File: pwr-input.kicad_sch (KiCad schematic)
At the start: 14 parts, among them J5 Conn_01x02, U6 TPS259472A

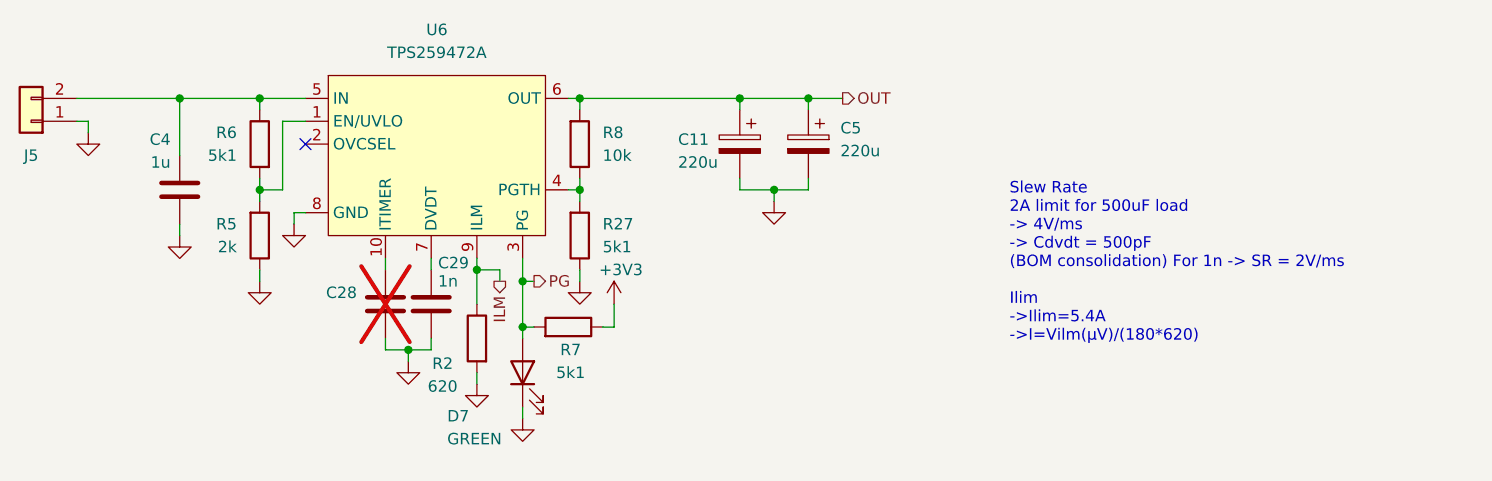
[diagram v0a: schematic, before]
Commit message: schem: add dual 5v pwr inputs
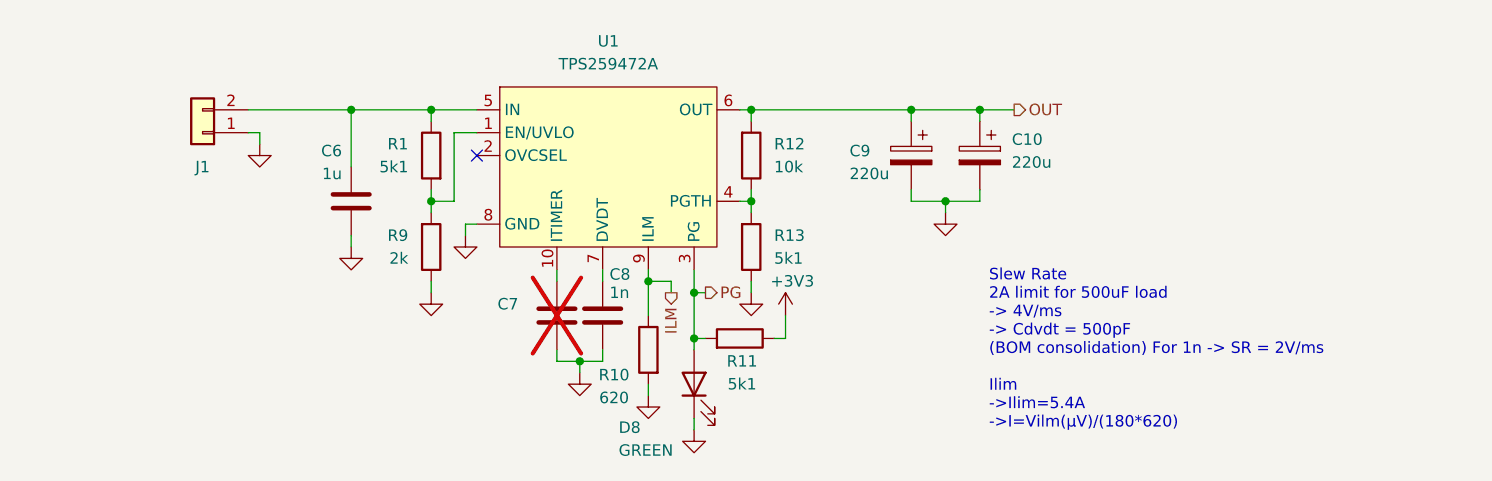
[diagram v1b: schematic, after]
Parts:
- renumbered C5 to C10, C4 to C6, C28 to C7, C29 to C8, C11 to C9, D7 to D8, J5 to J1, R6 to R1, R2 to R10, R7 to R11, R8 to R12, R27 to R13, R5 to R9, U6 to U1
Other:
- moved on the sheet: C10, C6, C7, C8, C9, D8, J1, R1, R10, R11, R12, R13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

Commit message: schem: run and fix ERC
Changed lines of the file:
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@@
+		(color 0 0 0 0)
+	)
+	(junction
+		(at 110.49 83.82)
+		(diameter 0)
 		(color 0 0 0 0)
 	)
@@
 	(wire
 		(pts
-			(xy 107.95 83.82) (xy 119.38 83.82)
+			(xy 107.95 83.82) (xy 110.49 83.82)
 		)
 		(stroke
@@
 		(pts
 			(xy 147.32 101.6) (xy 147.32 102.87)
+		)
+		(stroke
+			(width 0)
+			(type default)
+		)
+	)
+	(wire
+		(pts
+			(xy 110.49 83.82) (xy 119.38 83.82)
 		)
 		(stroke
@@
 					(unit 1)
 				)
+			)
+		)
+	)
+	(symbol
+		(lib_id "power:PWR_FLAG")
+		(at 110.49 83.82 0)
+		(unit 1)
+		(exclude_from_sim no)
+		(in_bom yes)
+		(on_board yes)
+		(dnp no)
+		(fields_autoplaced yes)
+		(property "Reference" "#FLG02"
+			(at 110.49 81.915 0)
+			(effects
+				(font
+					(size 1.27 1.27)
+				)
+				(hide yes)
+			)
+		)
+		(property "Value" "PWR_FLAG"
+			(at 110.49 78.74 0)
+			(effects
+				(font
+					(size 1.27 1.27)
+				)
+				(hide yes)
+			)
+		)
+		(property "Footprint" ""
+			(at 110.49 83.82 0)
+			(effects
+				(font
+					(size 1.27 1.27)
+				)
+				(hide yes)
+			)
+		)
+		(property "Datasheet" "~"
+			(at 110.49 83.82 0)
+			(effects
+				(font
+					(size 1.27 1.27)
+				)
+				(hide yes)
+			)
+		)
+		(property "Description" "Special symbol for telling ERC where power comes from"
+			(at 110.49 83.82 0)
+			(effects
+				(font
+					(size 1.27 1.27)
+				)
+				(hide yes)
+			)
+		)
+		(pin "1"
+		)
+		(instances
+			(project "valrob-carte-actionneurs-cdf-1"
+				(path "/6d04427e-e45e-4b7f-8323-501f87acc543/893ee43e-1e1d-4b28-9f3e-05e35ba62aed"
+					(reference "#FLG03")
+					(unit 1)
+				)
+				(path "/6d04427e-e45e-4b7f-8323-501f87acc543/fbcc9a91-3664-4a13-b680-428e68f2e4f4"
+					(reference "#FLG02")
+					(unit 1)
+				)

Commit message: schem: reannotate
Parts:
- renumbered C6 to C30, C7 to C31, C8 to C32, C9 to C33, C10 to C34, D8 to D26, J1 to J5, R1 to R13, R9 to R14, R10 to R15, R11 to R16, R12 to R17, R13 to R18, U1 to U4

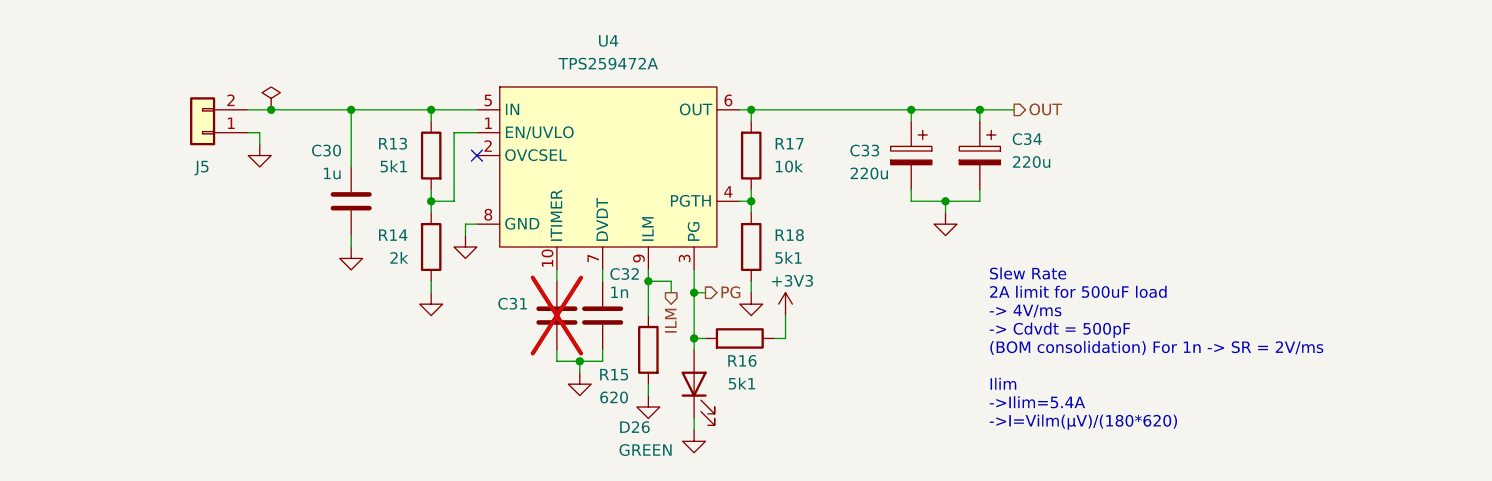
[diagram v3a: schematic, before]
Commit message: pcb: add 2x TPS25947 layout
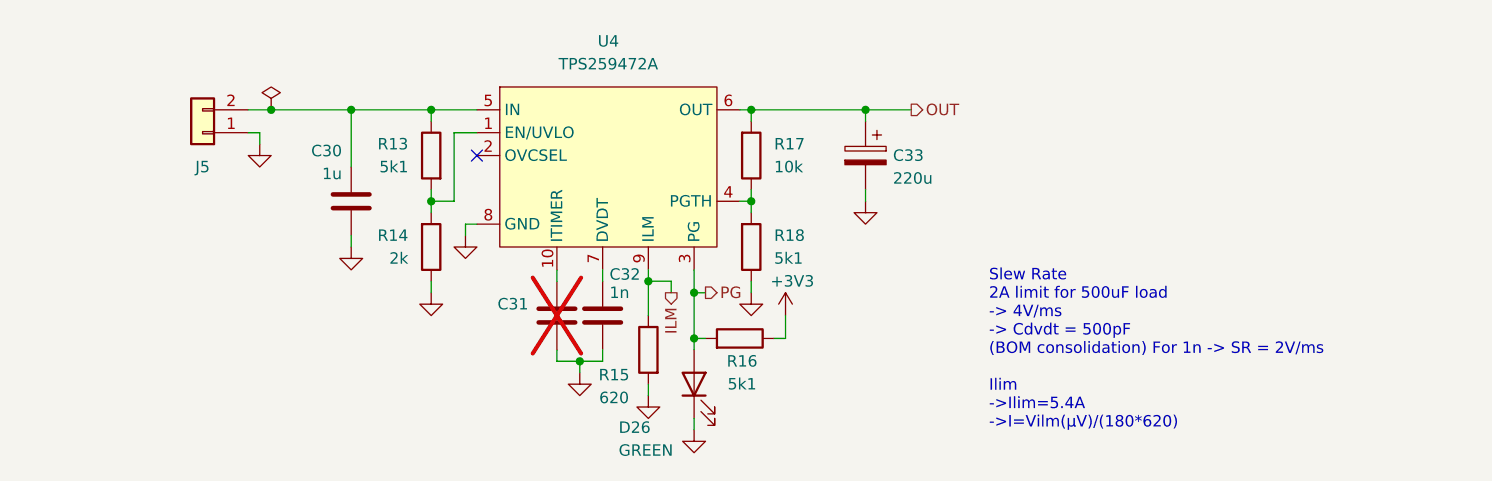
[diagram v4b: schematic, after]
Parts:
- removed C34: 220u, Capacitor_SMD:CP_Elec_6.3x7.7, symbol Device:C_Polarized
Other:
- moved on the sheet: C33
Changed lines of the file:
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@@
-	)
-	(junction
-		(at 181.61 83.82)
-		(diameter 0)
-		(color 0 0 0 0)
 	)
 	(junction
@@
 	)
 	(junction
-		(at 189.23 83.82)
-		(diameter 0)
-		(color 0 0 0 0)
-	)
-	(junction
 		(at 128.27 93.98)
 		(diameter 0)
@@
 	)
 	(junction
-		(at 185.42 93.98)
+		(at 176.53 83.82)
 		(diameter 0)
 		(color 0 0 0 0)
@@
 	(wire
 		(pts
-			(xy 189.23 93.98) (xy 189.23 92.71)
-		)
-		(stroke
-			(width 0)
-			(type default)
-		)
-	)
-	(wire
-		(pts
-			(xy 189.23 85.09) (xy 189.23 83.82)
-		)
-		(stroke
-			(width 0)
-			(type default)
-		)
-	)
-	(wire
-		(pts
 			(xy 128.27 92.71) (xy 128.27 93.98)
 		)
@@
 	(wire
 		(pts
-			(xy 181.61 92.71) (xy 181.61 93.98)
+			(xy 176.53 92.71) (xy 176.53 93.98)
 		)
 		(stroke
@@
 	(wire
 		(pts
-			(xy 181.61 93.98) (xy 185.42 93.98)
-		)
-		(stroke
-			(width 0)
-			(type default)
-		)
-	)
-	(wire
-		(pts
 			(xy 152.4 102.87) (xy 152.4 106.68)
 		)
@@
 	(wire
 		(pts
-			(xy 163.83 83.82) (xy 181.61 83.82)
+			(xy 163.83 83.82) (xy 176.53 83.82)
 		)
 		(stroke
@@
 	(wire
 		(pts
-			(xy 181.61 83.82) (xy 181.61 85.09)
+			(xy 176.53 83.82) (xy 176.53 85.09)
 		)
 		(stroke
@@
 	(wire
 		(pts
-			(xy 185.42 93.98) (xy 185.42 95.25)
+			(xy 176.53 83.82) (xy 181.61 83.82)
 		)
 		(stroke
@@
 	(wire
 		(pts
-			(xy 189.23 83.82) (xy 193.04 83.82)
-		)
-		(stroke
-			(width 0)
-			(type default)
-		)
-	)
-	(wire
-		(pts
 			(xy 133.35 86.36) (xy 130.81 86.36)
 		)
@@
 	(wire
 		(pts
-			(xy 185.42 93.98) (xy 189.23 93.98)
-		)
-		(stroke
-			(width 0)
-			(type default)
-		)
-	)
-	(wire
-		(pts
 			(xy 132.08 97.79) (xy 132.08 96.52)
 		)
@@
 		(pts
 			(xy 130.81 93.98) (xy 128.27 93.98)
-		)
-		(stroke
-			(width 0)
-			(type default)
-		)
-	)
-	(wire
-		(pts
-			(xy 181.61 83.82) (xy 189.23 83.82)
 		)
 		(stroke
@@
 	(hierarchical_label "OUT"
 		(shape output)
-		(at 193.04 83.82 0)
+		(at 181.61 83.82 0)
 		(effects
 			(font
@@
 	(symbol
 		(lib_id "power:GND")
-		(at 185.42 95.25 0)
+		(at 176.53 93.98 0)
 		(unit 1)
 		(exclude_from_sim no)
@@
 		(fields_autoplaced yes)
 		(property "Reference" "#PWR087"
-			(at 185.42 101.6 0)
+			(at 176.53 100.33 0)
 			(effects
 				(font
@@
 		)
 		(property "Value" "GND"
-			(at 185.42 100.33 0)
+			(at 176.53 99.06 0)
 			(effects
 				(font
@@
 		)
 		(property "Footprint" ""
-			(at 185.42 95.25 0)
+			(at 176.53 93.98 0)
 			(effects
 				(font
@@
 		)
 		(property "Datasheet" ""
-			(at 185.42 95.25 0)
+			(at 176.53 93.98 0)
 			(effects
 				(font
@@
 		)
 		(property "Description" "Power symbol creates a global label with name \"GND\" , ground"
-			(at 185.42 95.25 0)
+			(at 176.53 93.98 0)
 			(effects
 				(font
@@
 				(path "/6d04427e-e45e-4b7f-8323-501f87acc543/fbcc9a91-3664-4a13-b680-428e68f2e4f4"
 					(reference "#PWR078")
-					(unit 1)
-				)
-			)
-		)
-	)
-	(symbol
-		(lib_id "Device:C_Polarized")
-		(at 189.23 88.9 0)
-		(mirror y)
-		(unit 1)
-		(exclude_from_sim no)
-		(in_bom yes)
-		(on_board yes)
-		(dnp no)
-		(property "Reference" "C34"
-			(at 192.786 87.122 0)
-			(effects
-				(font
-					(size 1.27 1.27)
-				)
-				(justify right)
-			)
-		)
-		(property "Value" "220u"
-			(at 192.786 89.662 0)
-			(effects
-				(font
-					(size 1.27 1.27)
-				)
-				(justify right)
-			)
-		)
-		(property "Footprint" "Capacitor_SMD:CP_Elec_6.3x7.7"
-			(at 188.2648 92.71 0)
-			(effects
-				(font
-					(size 1.27 1.27)
-				)
-				(hide yes)
-			)
-		)
-		(property "Datasheet" "~"
-			(at 189.23 88.9 0)
-			(effects
-				(font
-					(size 1.27 1.27)
-				)
-				(hide yes)
-			)
-		)
-		(property "Description" "Polarized capacitor"
-			(at 189.23 88.9 0)
-			(effects
-				(font
-					(size 1.27 1.27)
-				)
-				(hide yes)
-			)
-		)
-		(property "Basic" "X"
-			(at 189.23 88.9 0)
-			(effects
-				(font
-					(size 1.27 1.27)
-				)
-				(hide yes)
-			)
-		)
-		(property "JLCPCB Part #" "C2918361"
-			(at 189.23 88.9 0)
-			(effects
-				(font
-					(size 1.27 1.27)
-				)
-				(hide yes)
-			)
-		)
-		(property "Manufacturer" "ROQANG"
-			(at 189.23 88.9 0)
-			(effects
-				(font
-					(size 1.27 1.27)
-				)
-				(hide yes)
-			)
-		)
-		(property "Manufacturer Part Number" "RVT1E221M0607"
-			(at 189.23 88.9 0)
-			(effects
-				(font
-					(size 1.27 1.27)
-				)
-				(hide yes)
-			)
-		)
-		(pin "2"
-		)
-		(pin "1"
-		)
-		(instances
-			(project "valrob-carte-actionneurs-cdf-1"
-				(path "/6d04427e-e45e-4b7f-8323-501f87acc543/893ee43e-1e1d-4b28-9f3e-05e35ba62aed"
-					(reference "C39")
-					(unit 1)
-				)
-				(path "/6d04427e-e45e-4b7f-8323-501f87acc543/fbcc9a91-3664-4a13-b680-428e68f2e4f4"
-					(reference "C34")
 					(unit 1)
 				)
@@
 	(symbol
 		(lib_id "Device:C_Polarized")
-		(at 181.61 88.9 0)
+		(at 176.53 88.9 0)
 		(mirror y)
 		(unit 1)
@@
 		(dnp no)
 		(property "Reference" "C33"
-			(at 174.752 88.392 0)
+			(at 179.578 88.9 0)
 			(effects
 				(font
@@
 		)
 		(property "Value" "220u"
-			(at 174.752 90.932 0)
+			(at 179.578 91.44 0)
 			(effects
 				(font
@@
 		)
 		(property "Footprint" "Capacitor_SMD:CP_Elec_6.3x7.7"
-			(at 180.6448 92.71 0)
+			(at 175.5648 92.71 0)
 			(effects
 				(font
@@
 		)
 		(property "Datasheet" "~"
-			(at 181.61 88.9 0)
+			(at 176.53 88.9 0)
 			(effects
 				(font
@@
 		)
 		(property "Description" "Polarized capacitor"
-			(at 181.61 88.9 0)
+			(at 176.53 88.9 0)
 			(effects
 				(font
@@
 		)
 		(property "Basic" "X"
-			(at 181.61 88.9 0)
+			(at 176.53 88.9 0)
 			(effects
 				(font
@@
 		)
 		(property "JLCPCB Part #" "C2918361"
-			(at 181.61 88.9 0)
+			(at 176.53 88.9 0)
 			(effects
 				(font
@@
 		)
 		(property "Manufacturer" "ROQANG"
-			(at 181.61 88.9 0)
+			(at 176.53 88.9 0)
 			(effects
 				(font
@@
 		)
 		(property "Manufacturer Part Number" "RVT1E221M0607"
-			(at 181.61 88.9 0)
-			(effects
-				(font
+			(at 176.53 88.9 0)
+			(effects
+				(font
